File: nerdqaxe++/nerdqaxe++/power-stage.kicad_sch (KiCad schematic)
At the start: 19 parts, among them U4 CSD95472Q5MC

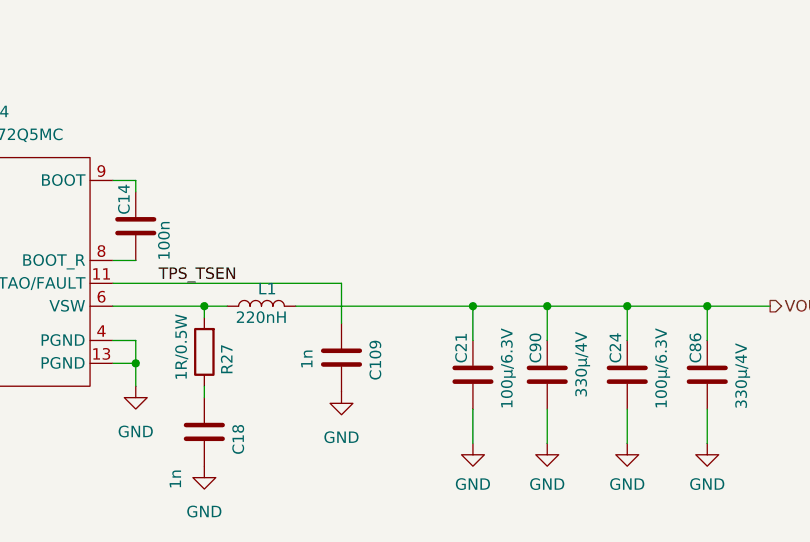
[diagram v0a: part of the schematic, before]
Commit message: fixed temp sensing connection to the buck on the ++
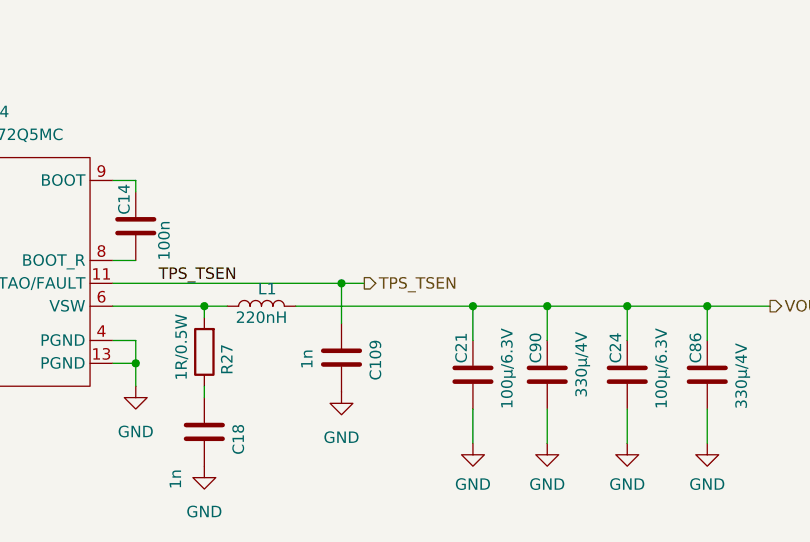
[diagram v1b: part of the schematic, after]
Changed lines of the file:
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@@
 		(color 0 0 0 0)
 	)
+	(junction
+		(at 169.545 103.505)
+		(diameter 0)
+		(color 0 0 0 0)
+	)
 	(wire
 		(pts
@@
 		(pts
 			(xy 108.585 48.26) (xy 108.585 49.53)
+		)
+		(stroke
+			(width 0)
+			(type default)
+		)
+	)
+	(wire
+		(pts
+			(xy 169.545 103.505) (xy 172.085 103.505)
 		)
 		(stroke
@@
 		)
 	)
+	(hierarchical_label "TPS_TSEN"
+		(shape output)
+		(at 172.085 103.505 0)
+		(fields_autoplaced yes)
+		(effects
+			(font
+				(size 1.27 1.27)
+			)
+			(justify left)
+		)
+	)

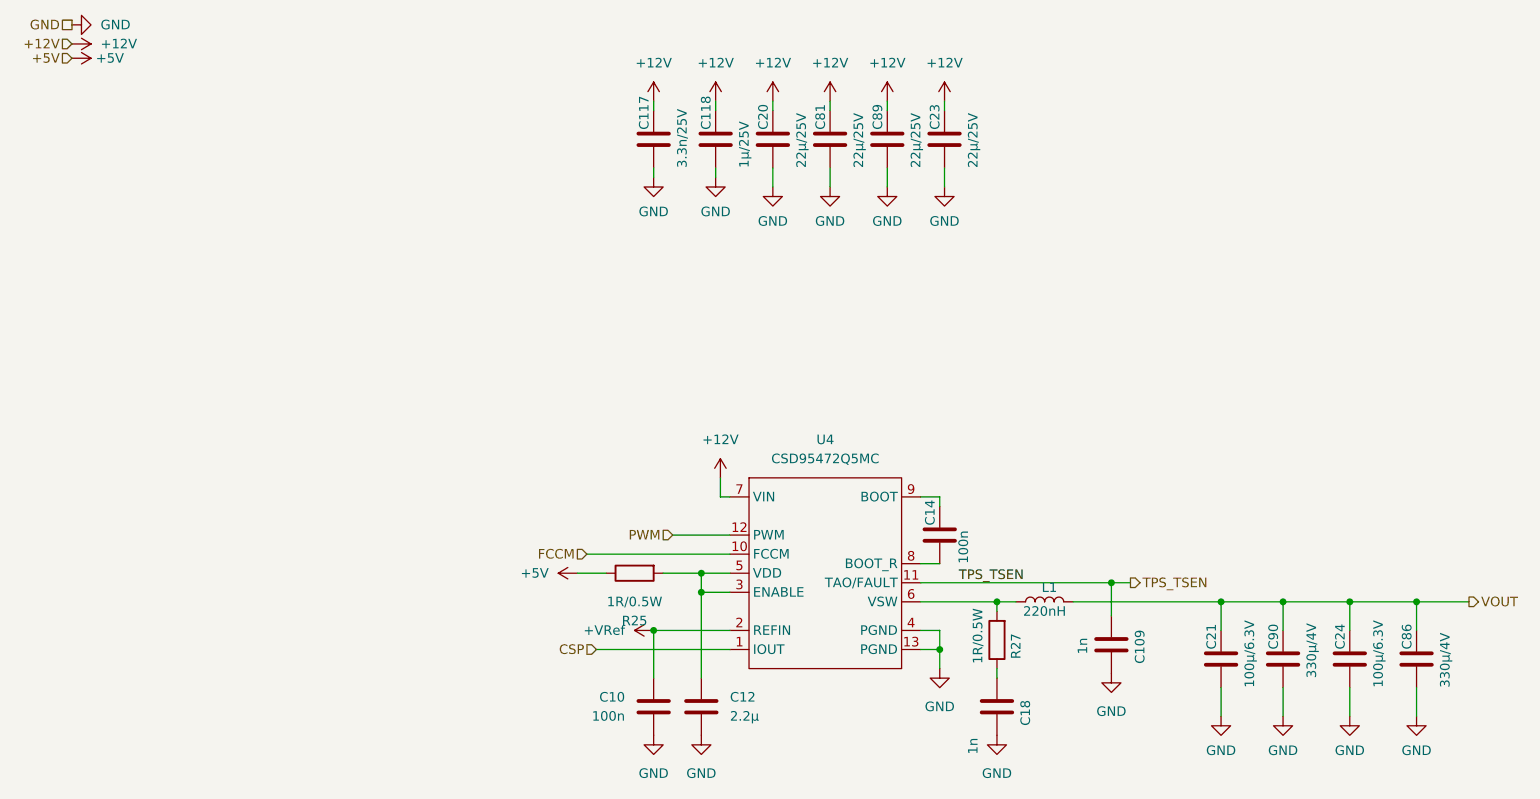
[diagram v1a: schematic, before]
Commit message: removed solderjumpers on ++
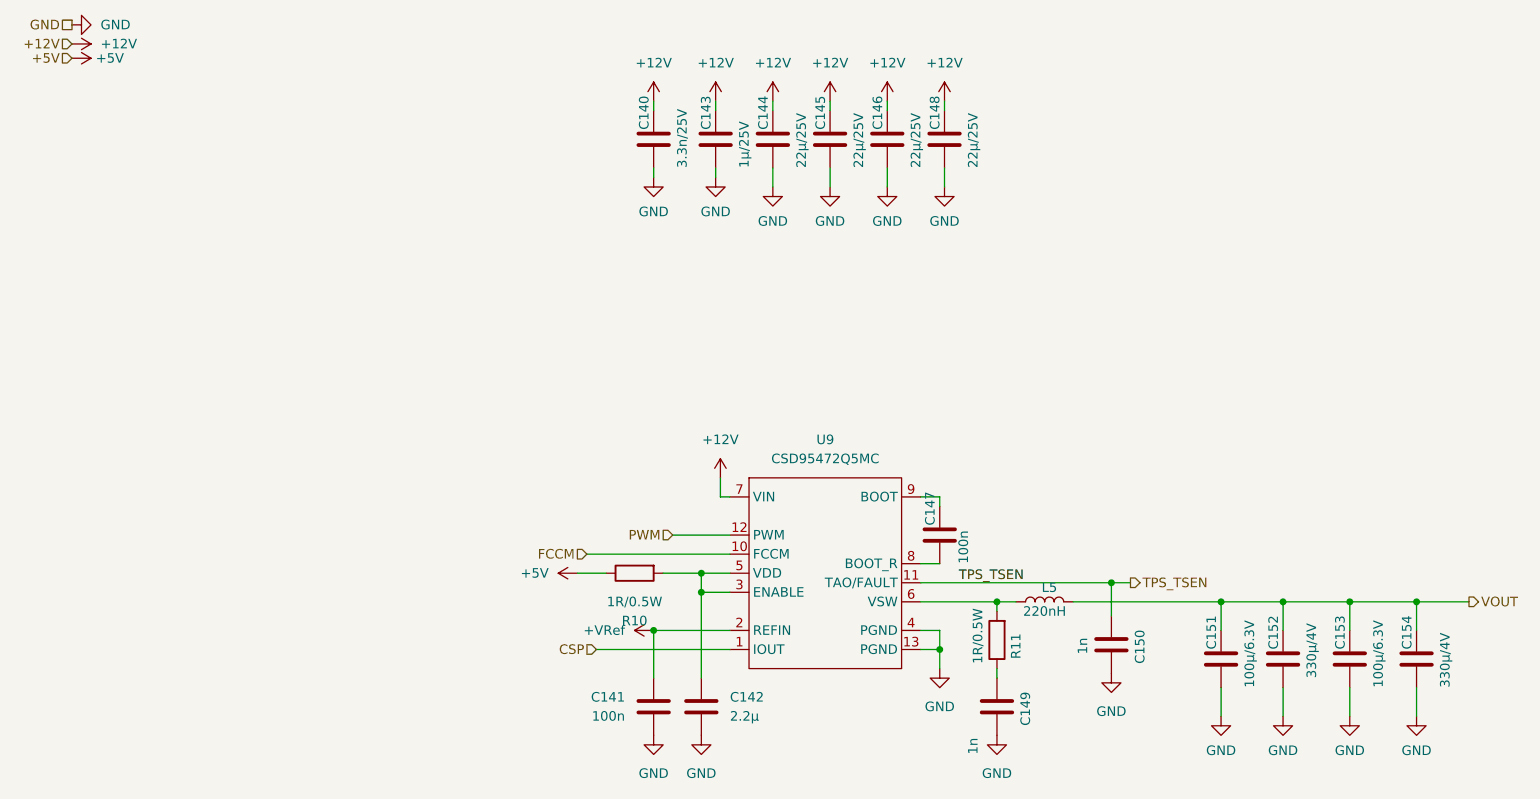
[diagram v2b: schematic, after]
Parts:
- C149: renamed from C18; value 1n -> 1n
- C150: renamed from C109; value 1n -> 1n
- renumbered C117 to C140, C10 to C141, C12 to C142, C118 to C143, C20 to C144, C81 to C145, C89 to C146, C14 to C147, C23 to C148, C21 to C151, C90 to C152, C24 to C153, C86 to C154, L1 to L5, R25 to R10, R27 to R11, U4 to U9
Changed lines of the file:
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@@
 (kicad_sch
-	(version 20231120)
+	(version 20250114)
 	(generator "eeschema")
-	(generator_version "8.0")
+	(generator_version "9.0")
 	(paper "A4")
 	(junction
@@
 	(label "TPS_TSEN"
 		(at 149.225 103.505 0)
-		(fields_autoplaced yes)
 		(effects
 			(font
@@
 		(shape output)
 		(at 217.17 106.045 0)
-		(fields_autoplaced yes)
 		(effects
 			(font
@@
 		(shape input)
 		(at 31.115 31.75 180)
-		(fields_autoplaced yes)
 		(effects
 			(font
@@
 		(shape input)
 		(at 100.965 112.395 180)
-		(fields_autoplaced yes)
 		(effects
 			(font
@@
 		(shape passive)
 		(at 31.115 29.21 180)
-		(fields_autoplaced yes)
 		(effects
 			(font
@@
 		(shape input)
 		(at 31.115 33.655 180)
-		(fields_autoplaced yes)
 		(effects
 			(font
@@
 		(shape input)
 		(at 111.125 97.155 180)
-		(fields_autoplaced yes)
 		(effects
 			(font
@@
 		(shape output)
 		(at 172.085 103.505 0)
-		(fields_autoplaced yes)
 		(effects
 			(font
@@
 		(shape input)
 		(at 99.695 99.695 180)
-		(fields_autoplaced yes)
 		(effects
 			(font
@@
 		(dnp no)
 		(fields_autoplaced yes)
-		(property "Reference" "#PWR0264"
+		(property "Reference" "#PWR0291"
 			(at 201.295 127.635 0)
 			(effects
@@
 		(dnp no)
 		(fields_autoplaced yes)
-		(property "Reference" "#PWR0259"
+		(property "Reference" "#PWR0266"
 			(at 37.465 29.21 0)
 			(effects
@@
 		(dnp no)
 		(fields_autoplaced yes)
-		(property "Reference" "#PWR053"
+		(property "Reference" "#PWR0284"
 			(at 146.685 121.285 0)
 			(effects
@@
 		(on_board yes)
 		(dnp no)
-		(property "Reference" "C21"
+		(property "Reference" "C151"
 			(at 182.88 112.395 90)
 			(effects
@@
 		(dnp no)
 		(fields_autoplaced yes)
-		(property "Reference" "#PWR0261"
+		(property "Reference" "#PWR0268"
 			(at 27.305 33.655 0)
 			(effects
@@
 		(on_board yes)
 		(dnp no)
-		(property "Reference" "C89"
+		(property "Reference" "C146"
 			(at 138.43 43.18 90)
 			(effects
@@
 		(on_board yes)
 		(dnp no)
-		(property "Reference" "R25"
+		(property "Reference" "R10"
 			(at 106.045 108.585 90)
 			(effects
@@
 		(dnp no)
 		(fields_autoplaced yes)
-		(property "Reference" "#PWR0262"
+		(property "Reference" "#PWR0289"
 			(at 184.15 127.635 0)
 			(effects
@@
 		(dnp no)
 		(fields_autoplaced yes)
-		(property "Reference" "#PWR0145"
+		(property "Reference" "#PWR0279"
 			(at 124.46 57.15 0)
 			(effects
@@
 		(dnp no)
 		(fields_autoplaced yes)
-		(property "Reference" "#PWR0217"
+		(property "Reference" "#PWR0288"
 			(at 169.545 121.92 0)
 			(effects
@@
 		(on_board yes)
 		(dnp no)
-		(property "Reference" "L1"
+		(property "Reference" "L5"
 			(at 161.29 104.14 90)
 			(effects
@@
 		(dnp no)
 		(fields_autoplaced yes)
-		(property "Reference" "#PWR0142"
+		(property "Reference" "#PWR0287"
 			(at 154.305 130.175 0)
 			(effects
@@
 		(dnp no)
 		(fields_autoplaced yes)
-		(property "Reference" "#PWR043"
+		(property "Reference" "#PWR0272"
 			(at 112.395 109.855 0)
 			(effects
@@
 		(on_board yes)
 		(dnp no)
-		(property "Reference" "C86"
+		(property "Reference" "C154"
 			(at 208.915 112.395 90)
 			(effects
@@
 		(on_board yes)
 		(dnp no)
-		(property "Reference" "C109"
+		(property "Reference" "C150"
 			(at 173.355 114.3 90)
 			(effects
@@
 			)
 		)
-		(property "Value" "1n "
+		(property "Value" "1n"
 			(at 165.735 113.03 90)
 			(effects
@@
 		(on_board yes)
 		(dnp no)
-		(property "Reference" "C81"
+		(property "Reference" "C145"
 			(at 130.81 43.18 90)
 			(effects
@@
 		(dnp no)
 		(fields_autoplaced yes)
-		(property "Reference" "#PWR0146"
+		(property "Reference" "#PWR0280"
 			(at 132.08 43.18 0)
 			(effects
@@
 		(dnp no)
 		(fields_autoplaced yes)
-		(property "Reference" "#PWR0260"
+		(property "Reference" "#PWR0267"
 			(at 27.305 31.75 0)
 			(effects
@@
 		(on_board yes)
 		(dnp no)
-		(property "Reference" "C23"
+		(property "Reference" "C148"
 			(at 146.05 43.18 90)
 			(effects
@@
 		(on_board yes)
 		(dnp no)
-		(property "Reference" "C24"
+		(property "Reference" "C153"
 			(at 200.025 112.395 90)
 			(effects
@@
 		(on_board yes)
 		(dnp no)
-		(property "Reference" "C18"
+		(property "Reference" "C149"
 			(at 158.115 122.555 90)
 			(effects
@@
 			)
 		)
-		(property "Value" "1n "
+		(property "Value" "1n"
 			(at 151.13 126.365 90)
 			(effects
@@
 		(dnp no)
 		(fields_autoplaced yes)
-		(property "Reference" "#PWR0230"
+		(property "Reference" "#PWR0275"
 			(at 116.84 43.18 0)
 			(effects
@@
 		(on_board yes)
 		(dnp no)
-		(property "Reference" "C14"
+		(property "Reference" "C147"
 			(at 145.415 95.885 90)
 			(effects
@@
 		(on_board yes)
 		(dnp no)
-		(property "Reference" "C20"
+		(property "Reference" "C144"
 			(at 123.19 43.18 90)
 			(effects
@@
 		(dnp no)
 		(fields_autoplaced yes)
-		(property "Reference" "#PWR0154"
+		(property "Reference" "#PWR0282"
 			(at 139.7 43.18 0)
 			(effects
@@
 		(on_board yes)
 		(dnp no)
-		(property "Reference" "C90"
+		(property "Reference" "C152"
 			(at 191.135 112.395 90)
 			(effects
@@
 		(on_board yes)
 		(dnp no)
-		(property "Reference" "C117"
+		(property "Reference" "C140"
 			(at 107.315 43.18 90)
 			(effects
@@
 		(dnp no)
 		(fields_autoplaced yes)
-		(property "Reference" "C12"
+		(property "Reference" "C142"
 			(at 118.745 118.7449 0)
 			(effects
@@
 		(dnp no)
 		(fields_autoplaced yes)
-		(property "Reference" "#PWR0155"
+		(property "Reference" "#PWR0283"
 			(at 139.7 57.15 0)
 			(effects
@@
 		(dnp no)
 		(fields_autoplaced yes)
-		(property "Reference" "#PWR044"
+		(property "Reference" "#PWR0273"
 			(at 108.585 130.175 0)
 			(effects
@@
 		(dnp no)
 		(fields_autoplaced yes)
-		(property "Reference" "#PWR0229"
+		(property "Reference" "#PWR0271"
 			(at 108.585 55.88 0)
 			(effects
@@
 		(dnp no)
 		(fields_autoplaced yes)
-		(property "Reference" "U4"
+		(property "Reference" "U9"
 			(at 131.445 84.455 0)
 			(effects
@@
 		(on_board yes)
 		(dnp no)
-		(property "Reference" "C118"
+		(property "Reference" "C143"
 			(at 115.57 43.18 90)
 			(effects
@@
 		(dnp no)
 		(fields_autoplaced yes)
-		(property "Reference" "#PWR0265"
+		(property "Reference" "#PWR0292"
 			(at 210.185 127.635 0)
 			(effects
@@
 		(dnp no)
 		(fields_autoplaced yes)
-		(property "Reference" "#PWR047"
+		(property "Reference" "#PWR0274"
 			(at 114.935 130.175 0)
 			(effects
@@
 		(dnp no)
 		(fields_autoplaced yes)
-		(property "Reference" "#PWR0263"
+		(property "Reference" "#PWR0290"
 			(at 192.405 127.635 0)
 			(effects
@@
 		(dnp no)
 		(fields_autoplaced yes)
-		(property "Reference" "#PWR0147"
+		(property "Reference" "#PWR0281"
 			(at 132.08 57.15 0)
 			(effects
@@
 		(dnp no)
 		(fields_autoplaced yes)
-		(property "Reference" "#PWR0159"
+		(property "Reference" "#PWR0285"
 			(at 147.32 43.18 0)
 			(effects
@@
 		(dnp no)
 		(fields_autoplaced yes)
-		(property "Reference" "#PWR0160"
+		(property "Reference" "#PWR0286"
 			(at 147.32 57.15 0)
 			(effects
@@
 		(dnp no)
 		(fields_autoplaced yes)
-		(property "Reference" "#PWR0228"
+		(property "Reference" "#PWR0270"
 			(at 108.585 43.18 0)
 			(effects
@@
 		(dnp no)
 		(fields_autoplaced yes)
-		(property "Reference" "#PWR049"
+		(property "Reference" "#PWR0277"
 			(at 117.475 93.345 0)
 			(effects
@@
 		(dnp no)
 		(fields_autoplaced yes)
-		(property "Reference" "#PWR041"
+		(property "Reference" "#PWR0269"
 			(at 102.235 102.235 0)
 			(effects
@@
 		(on_board yes)
 		(dnp no)
-		(property "Reference" "R27"
+		(property "Reference" "R11"
 			(at 156.845 113.665 90)
 			(effects
@@
 		(dnp no)
 		(fields_autoplaced yes)
-		(property "Reference" "#PWR0235"
+		(property "Reference" "#PWR0276"
 			(at 116.84 55.88 0)
 			(effects
@@
 		(dnp no)
 		(fields_autoplaced yes)
-		(property "Reference" "#PWR0144"
+		(property "Reference" "#PWR0278"
 			(at 124.46 43.18 0)
 			(effects
@@
 		(on_board yes)
 		(dnp no)
-		(property "Reference" "C10"
+		(property "Reference" "C141"
 			(at 104.775 118.7449 0)
 			(effects

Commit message: rev5.1.1
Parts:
- C140: Distributor (none) -> D; Manufacturer (none) -> C0805C332J1GEC7210; OrderNr (none) -> 399-C0805C332J1GEC7210CT-ND; temp-coefficient (none) -> C0G
- C141, C147: Distributor (none) -> D; Manufacturer (none) -> C0805C104K5RACTU; OrderNr (none) -> 399-C0805C104K5RACTUCT-ND; temp-coefficient (none) -> X7R
- C142: Distributor (none) -> D; Manufacturer (none) -> UMK212BB7225KG-T; OrderNr (none) -> 587-3169-1-ND; temp-coefficient (none) -> X7R
- C143: Distributor (none) -> D; Manufacturer (none) -> CL21B105KBFNNNE; OrderNr (none) -> 1276-1029-1-ND; temp-coefficient (none) -> X7R
- C144, C145, C146, C148: Manufacturer C1210C226K3PAC7800 -> CL32B226KAJNNNE; OrderNr 399-C1210C226K3PAC7800CT-ND -> 1276-3392-1-ND; temp-coefficient (none) -> X7R
- C149: value 1n -> 2.7n; Distributor (none) -> D; Manufacturer (none) -> C0805C272JAGACTU; OrderNr (none) -> 399-C0805C272JAGACTUCT-ND; temp-coefficient (none) -> C0G
- C150: Distributor (none) -> D; Manufacturer (none) -> C0805C102J2GECTU; OrderNr (none) -> 399-C0805C102J2GECTUCT-ND; temp-coefficient (none) -> C0G
- C151, C153: value 100µ/6.3V -> 100µ/10V; temp-coefficient (none) -> X5R
- C152, C154: temp-coefficient (none) -> X5R
